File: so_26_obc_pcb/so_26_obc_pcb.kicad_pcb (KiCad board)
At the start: 4 copper layers, 90.2 x 95.9 mm, 52 parts, among them J1 Conn_02x12_Odd_Even, J2 Conn_02x06_Odd_Even, J3 Conn_01x04, J4 Conn_01x03, J5 Conn_01x02, J6 Conn_01x03, J7 Conn_01x03, J8 Conn_01x03, J9 Conn_01x02, SW1 SW_Push, U1 STM32G431RBTx, U2 TPT3232A-TS3R, U3 PCT2075, U4 MPRLS0025, U5 LSM6DS3, U6 MEM2067-02-180-00-A

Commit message: PCB: Gave routing a couple of componentsone more try
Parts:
- moved U6 88.4 mm to (145.1, 114.7), turned to 90 degrees
- moved J8 81.1 mm to (60.4, 120.1)
- moved J4 81.1 mm to (60.5, 109.7)
- moved U4 56.9 mm to (78.5, 138.4), turned to 90 degrees
- moved R9 52.5 mm to (125.1, 106.6), turned to 90 degrees
- moved R11 50.3 mm to (125.2, 123.5), turned to 180 degrees
- moved C17 49.7 mm to (125.1, 110.9), turned to 0 degrees
- moved C21 49.2 mm to (81.7, 134.3), turned to 180 degrees
- moved C19 49.0 mm to (125.2, 120.3), turned to 0 degrees
- moved R8 48.8 mm to (125.2, 113.7), turned to 180 degrees
- moved R10 48.5 mm to (125.2, 117.0), turned to 180 degrees
- moved C18 40.6 mm to (81.8, 125.5), turned to 180 degrees
- moved C13 36.8 mm to (77.9, 101.7), turned to -90 degrees
- moved U3 35.7 mm to (72.8, 101.7), turned to 0 degrees
- moved C11 32.3 mm to (128.9, 62.7)
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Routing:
- net +3V3: track 484.6 -> 23.4 mm, vias 5 -> 0
- net GND: track 127.5 -> 0.05 mm, vias 70 -> 0
- net /VBAT_0: track 68.8 -> 0.00 mm, vias 2 -> 0
- net /VBAT_1: track 66.4 -> 0.00 mm, vias 2 -> 0
- net /PWM_HEATER: track 99.8 -> 34.9 mm
- net /SD_CS: track 49.1 -> 0.00 mm, vias 2 -> 0
- net /DEBUG_UART_TX: track 39.6 -> 0.00 mm
- net ALT_+10V: track 43.5 -> 5.08 mm
- net /BOOT0: track 217.0 -> 182.6 mm, vias 7 -> 8
- net /NRST: track 86.7 -> 53.3 mm
- net /SD_MOSI: track 66.6 -> 34.6 mm, vias 2 -> 0
- net /RADIO_UART_RX: track 77.6 -> 48.7 mm, vias 2 -> 4
- net /LOW_POWER_MODE: track 76.7 -> 50.6 mm
- net /SD_SCK: track 67.0 -> 41.0 mm, vias 2 -> 0
- net /RADIO_UART_TX: track 75.4 -> 49.6 mm, vias 2 -> 4
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
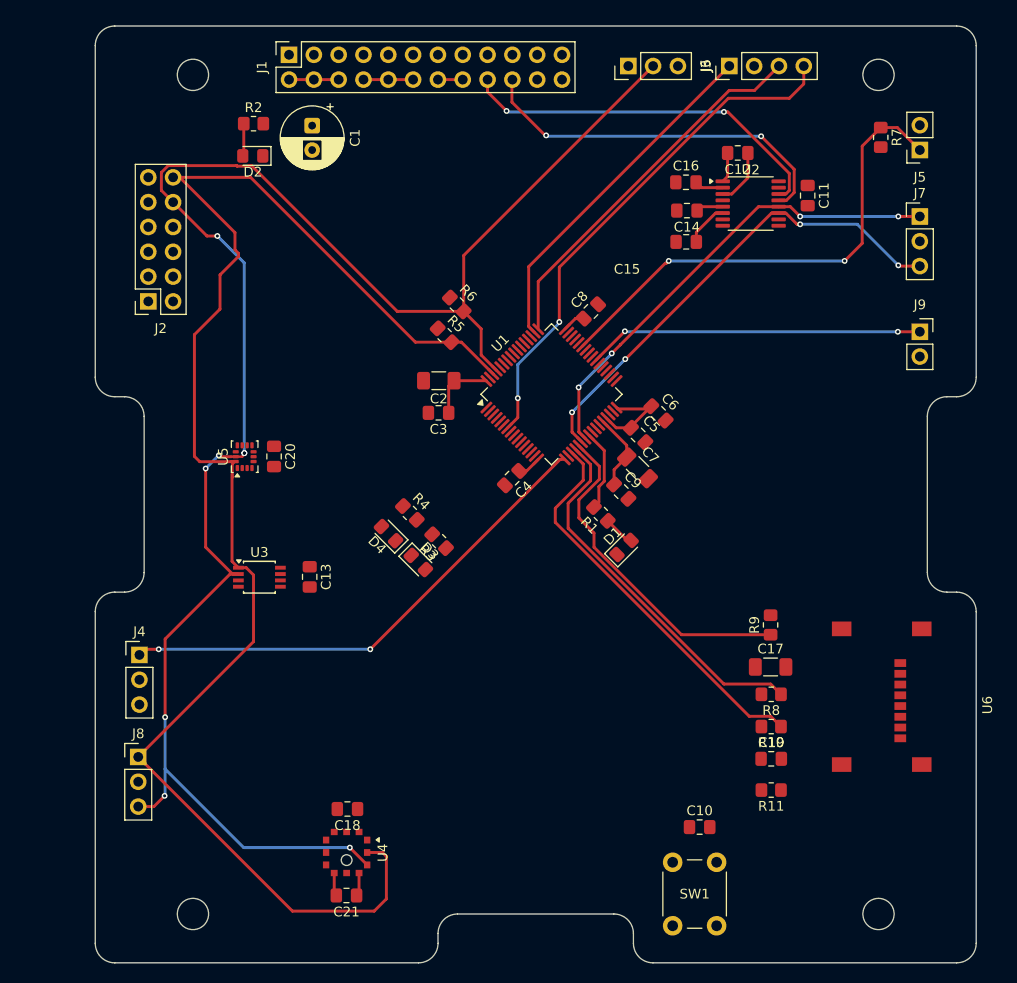
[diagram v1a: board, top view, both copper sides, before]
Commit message: PCB: Routed before cleanup by AJ
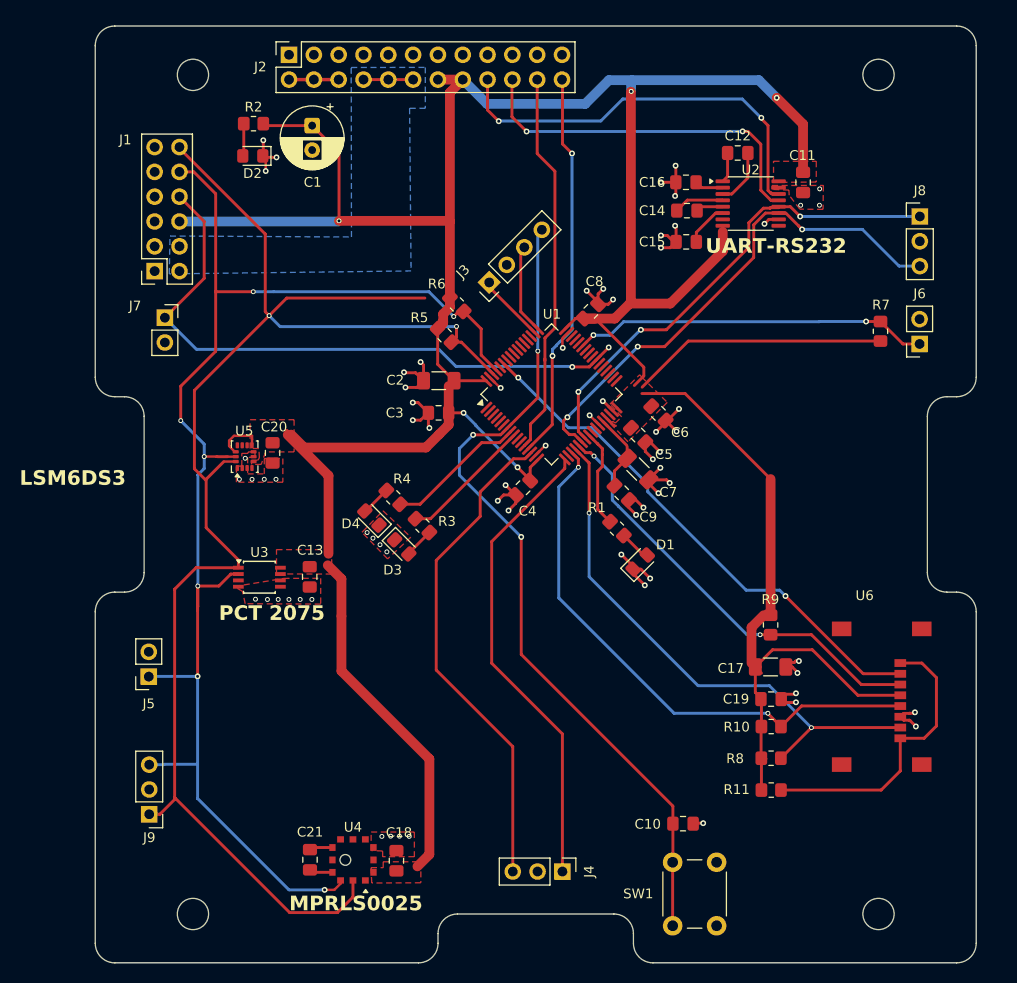
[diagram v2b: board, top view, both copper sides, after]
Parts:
- removed the J6 at (110.6, 49.4)
- added J5: Conn_01x02, Connector_PinSocket_2.54mm:PinSocket_1x02_P2.54mm_Vertical, F.Cu at (61.5, 111.9)
- moved J7 77.3 mm to (63.1, 75.2)
- moved J4 48.6 mm to (103.8, 131.8), turned to -90 degrees
- moved J3 33.1 mm to (96.3, 71.5), turned to 135 degrees
- moved J6 19.9 mm to (140.4, 77.8)
- moved R7 19.9 mm to (136.4, 76.5)
- moved U4 11.9 mm to (73.9, 127.4), turned to 0 degrees
- moved C18 7.29 mm to (86.8, 130.7), turned to 90 degrees
- moved R8 6.54 mm to (125.2, 120.2)
- moved C19 6.11 mm to (125.2, 114.2)
- moved J9 5.98 mm to (61.5, 126.0), turned to 180 degrees
- moved C21 5.23 mm to (78.0, 130.6), turned to 90 degrees
- moved J1 3.17 mm to (62.1, 70.4)
- moved R3 2.33 mm to (89.5, 96.4)
- moved R4 2.33 mm to (86.5, 93.5)
- moved D3 2.33 mm to (87.4, 98.6)
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- renumbered J2 to J1, J1 to J2, J5 to J6, J9 to J7, J7 to J8, J8 to J9
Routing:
- net +3V3: track 23.4 -> 375.4 mm, vias 0 -> 5
- net GND: track 0.05 -> 83.8 mm, vias 0 -> 69
- net /SD_CS: track 0.00 -> 54.2 mm, vias 0 -> 2
- net /DEBUG_UART_TX: track 0.00 -> 50.9 mm
- net /VBAT_1: track 0.00 -> 40.1 mm, vias 0 -> 2
- net /VBAT_0: track 0.00 -> 39.7 mm
- net /BOOT0: track 182.6 -> 143.8 mm, vias 8 -> 7
- net /NRST: track 53.3 -> 85.4 mm, vias 2 -> 3
- net /PWM_HEATER: track 34.9 -> 64.9 mm
- net Net-(U6-DAT1): track 0.00 -> 29.9 mm
- net /SWDIO: track 39.1 -> 9.27 mm
- net /SWCLK: track 36.1 -> 7.07 mm
- net /SD_MISO: track 38.6 -> 56.9 mm, vias 0 -> 2
- net /SD_SCK: track 41.0 -> 57.7 mm, vias 0 -> 2
- net /LED_GREEN: track 0.00 -> 14.4 mm
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- added copper zone on F.Cu, net +3V3
- added copper zone on B.Cu, net ALT_+10V
- added copper zone on F.Cu, net GND
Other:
- board text added: "LSM6DS3"
- board text added: "MPRLS0025"
- board text added: "PCT 2075"
- board text added: "Regine Angermo Birkely SubOrbital 25/26 Orbit NTNU"
- board text added: "SO_25/26_ OBC_PCB 11.02.26 Rev. 1"
- board text added: "UART-RS232"

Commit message: PCB: final routing + review
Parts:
- moved J10 51.9 mm to (90.5, 68.9), turned to 135 degrees
- moved SW1 51.7 mm to (93.1, 90.7), turned to -135 degrees
- moved C10 45.4 mm to (94.5, 87.1), turned to 135 degrees
- moved R4 40.3 mm to (97.8, 132.2), turned to 90 degrees
- moved R3 38.2 mm to (103.1, 132.2), turned to 90 degrees
- moved D4 38.1 mm to (95.2, 132.2), turned to -90 degrees
- moved D3 36.0 mm to (100.5, 132.2), turned to -90 degrees
- moved R1 35.5 mm to (108.3, 132.2), turned to 90 degrees
- moved D1 32.6 mm to (105.7, 132.2), turned to -90 degrees
- moved J8 31.4 mm to (65.5, 94.8)
- moved J4 30.8 mm to (95.1, 102.3)
- moved R7 24.3 mm to (112.1, 74.9), turned to -135 degrees
- moved C3 22.2 mm to (113.3, 83.5), turned to 0 degrees
- moved J7 21.7 mm to (120.1, 57.4), turned to -90 degrees
- moved C2 17.3 mm to (104.4, 70.5), turned to 45 degrees
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- renumbered J2 to J1, J5 to J10, J1 to J2, J6 to J5, J8 to J7, J9 to J8, J7 to J9
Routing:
- net +3V3: track 375.4 -> 294.5 mm, vias 5 -> 0
- net /NRST: track 85.4 -> 29.6 mm, vias 3 -> 0
- net /I2C_SDA: track 157.2 -> 114.0 mm, vias 2 -> 3
- net /LED_BLUE: track 10.1 -> 46.6 mm, vias 0 -> 2
- net /LED_YELLOW: track 13.6 -> 47.3 mm
- net /LED_GREEN: track 14.4 -> 46.7 mm
- net /DEBUG_UART_RX: track 48.3 -> 16.4 mm, vias 0 -> 1
- net GND: track 83.8 -> 52.7 mm, vias 69 -> 87
- net /DEBUG_UART_TX: track 50.9 -> 21.4 mm, vias 0 -> 1
- net /SWDIO: track 9.27 -> 20.4 mm
- net /RADIO_TX: track 42.3 -> 31.9 mm, vias 2 -> 1
- net /BOOT0: track 143.8 -> 134.4 mm, vias 7 -> 3
- net /SD_MISO: track 56.9 -> 63.9 mm
- net /RADIO_RX: track 37.4 -> 30.4 mm, vias 2 -> 1
- net /RADIO_UART_RX: track 49.9 -> 43.5 mm, vias 3 -> 2
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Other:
- board text added: "+3V3"
- board text added: "3V3"
- board text added: "ALT_+10V"
- board text added: "DEBUG_UART_RX"
- board text added: "DEBUG_UART_TX"
- board text added: "GND"
- board text added: "I2C"
- board text added: "LOW_POWER_MODE"
- board text added: "NRST"
- board text added: "PWM"
- board text added: "RADIO_UART_RX"
- board text added: "RADIO_UART_TX"
- board text added: "RESET"
- board text added: "SCL"
- board text added: "SDA"
- board text added: "SO26 - OBC Rev 1 Regine Angermo Birkely 11.02.26"
- board text added: "SWDIO"
- board text added: "SWLCK"
- board text removed: "Regine Angermo Birkely SubOrbital 25/26 Orbit NTNU"
- board text removed: "SO_25/26_ OBC_PCB 11.02.26 Rev. 1"

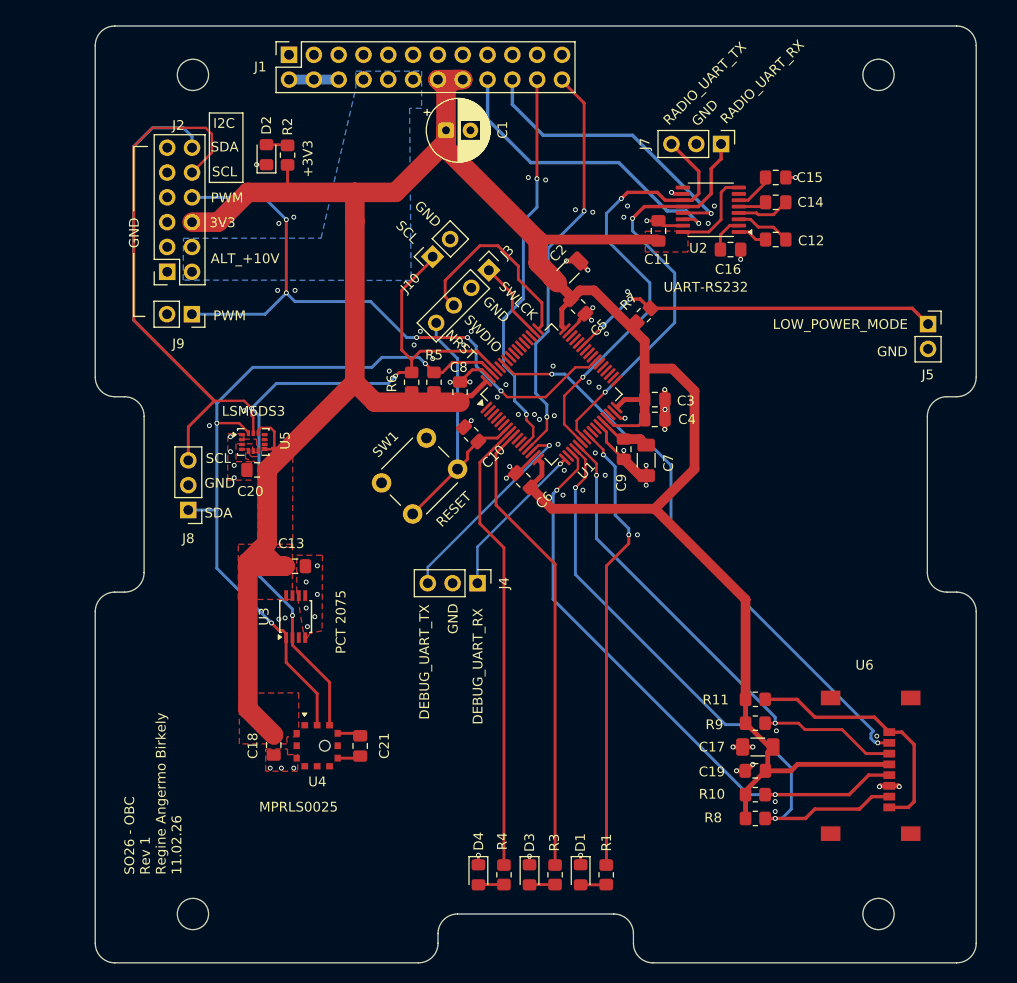
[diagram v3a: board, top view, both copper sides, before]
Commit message: stiching vias added
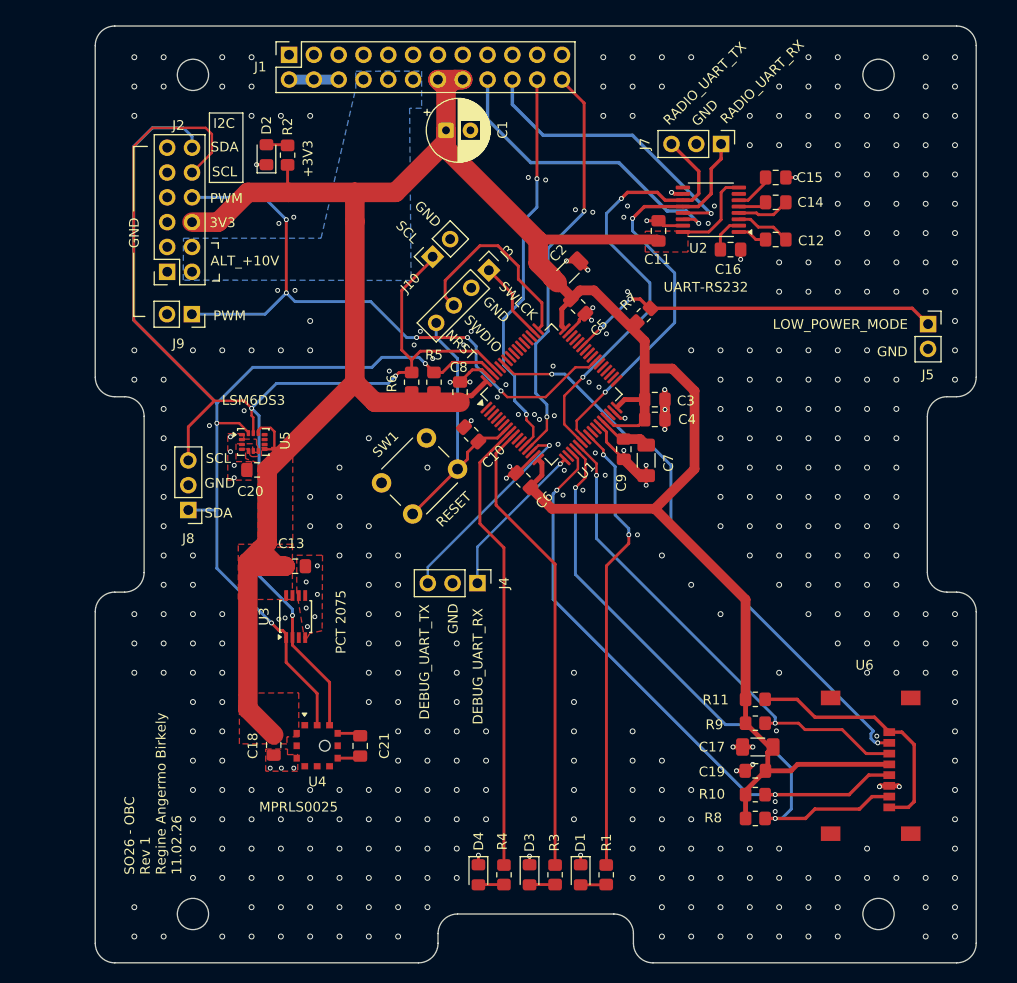
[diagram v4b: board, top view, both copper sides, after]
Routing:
- net GND: vias 87 -> 429
